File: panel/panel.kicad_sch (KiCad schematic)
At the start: 22 parts

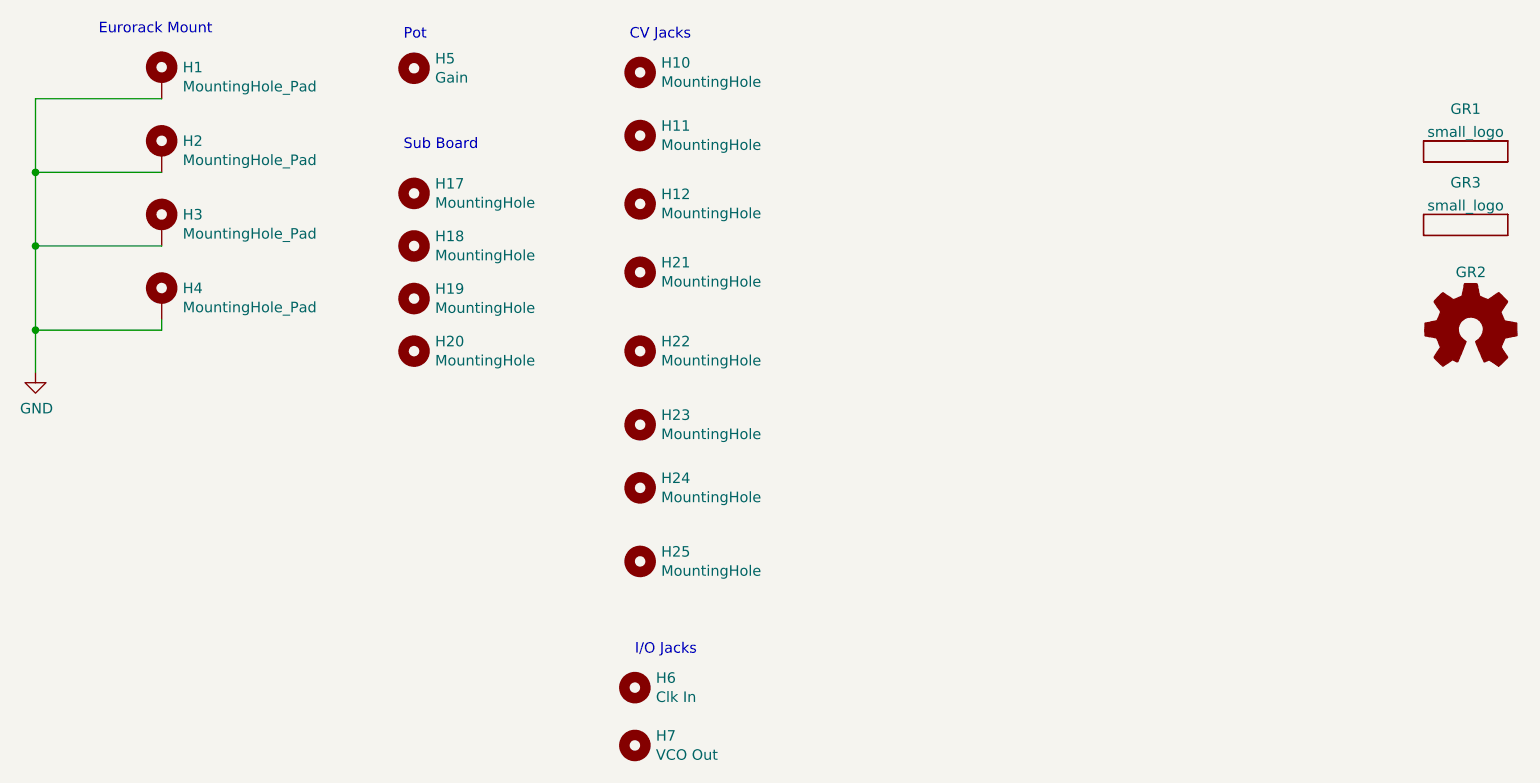
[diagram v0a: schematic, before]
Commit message: Adds harmonic outputs
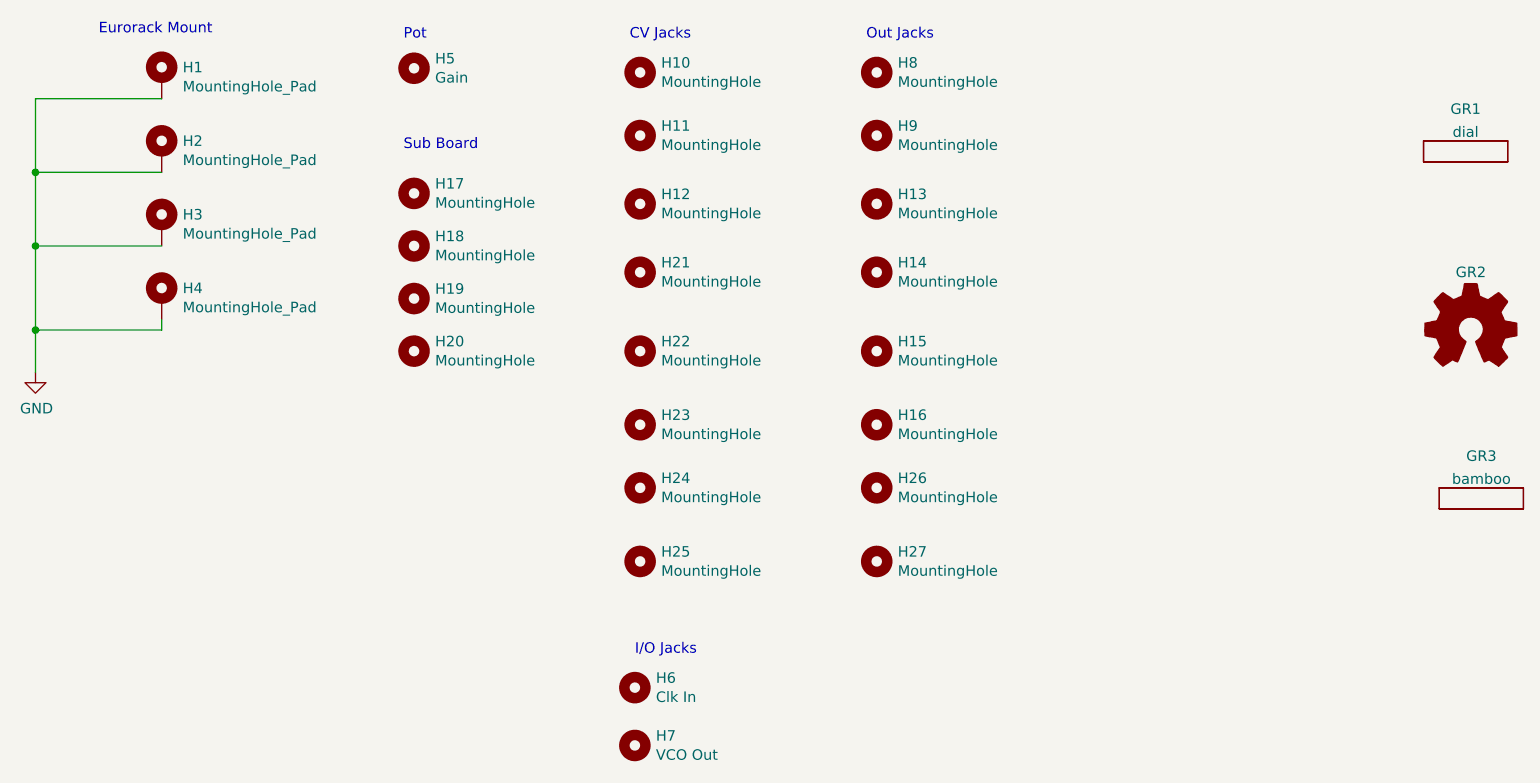
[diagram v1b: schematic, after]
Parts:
- added H13, H14, H15, H16, H26, H27, H8, H9: MountingHole, panel:MolexJack, symbol Mechanical:MountingHole
- GR1: value small_logo -> dial; footprint panel:small_face -> panel:dial_sm
- GR3: value small_logo -> bamboo; footprint Symbol:KiCad-Logo_5mm_SilkScreen -> panel:bambooh
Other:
- note added: "Out Jacks"
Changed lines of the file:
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@@
+    (effects (font (size 1.27 1.27)) (justify left bottom))
+  )
+  (text "Out Jacks" (at 158.75 48.26 0)
     (effects (font (size 1.27 1.27)) (justify left bottom))
   )
@@
     )
   )
+  (symbol (lib_id "Mechanical:MountingHole") (at 160.02 102.235 0) (unit 1)
+    (in_bom yes) (on_board yes)
+    (property "Reference" "H26" (id 0) (at 162.56 101.0666 0)
+      (effects (font (size 1.27 1.27)) (justify left))
+    )
+    (property "Value" "MountingHole" (id 1) (at 162.56 103.378 0)
+      (effects (font (size 1.27 1.27)) (justify left))
+    )
+    (property "Footprint" "panel:MolexJack" (id 2) (at 160.02 102.235 0)
+      (effects (font (size 1.27 1.27)) hide)
+    )
+    (property "Datasheet" "~" (id 3) (at 160.02 102.235 0)
+      (effects (font (size 1.27 1.27)) hide)
+    )
+  )
   (symbol (lib_id "Mechanical:MountingHole_Pad") (at 73.66 52.705 0) (unit 1)
     (in_bom yes) (on_board yes)
@@
     )
   )
+  (symbol (lib_id "Mechanical:MountingHole") (at 160.02 52.07 0) (unit 1)
+    (in_bom yes) (on_board yes)
+    (property "Reference" "H8" (id 0) (at 162.56 50.9016 0)
+      (effects (font (size 1.27 1.27)) (justify left))
+    )
+    (property "Value" "MountingHole" (id 1) (at 162.56 53.213 0)
+      (effects (font (size 1.27 1.27)) (justify left))
+    )
+    (property "Footprint" "panel:MolexJack" (id 2) (at 160.02 52.07 0)
+      (effects (font (size 1.27 1.27)) hide)
+    )
+    (property "Datasheet" "~" (id 3) (at 160.02 52.07 0)
+      (effects (font (size 1.27 1.27)) hide)
+    )
+  )
   (symbol (lib_id "Mechanical:MountingHole") (at 104.14 79.375 0) (unit 1)
     (in_bom yes) (on_board yes)
@@
     )
   )
+  (symbol (lib_id "Mechanical:MountingHole") (at 160.02 67.945 0) (unit 1)
+    (in_bom yes) (on_board yes)
+    (property "Reference" "H13" (id 0) (at 162.56 66.7766 0)
+      (effects (font (size 1.27 1.27)) (justify left))
+    )
+    (property "Value" "MountingHole" (id 1) (at 162.56 69.088 0)
+      (effects (font (size 1.27 1.27)) (justify left))
+    )
+    (property "Footprint" "panel:MolexJack" (id 2) (at 160.02 67.945 0)
+      (effects (font (size 1.27 1.27)) hide)
+    )
+    (property "Datasheet" "~" (id 3) (at 160.02 67.945 0)
+      (effects (font (size 1.27 1.27)) hide)
+    )
+  )
   (symbol (lib_id "Mechanical:MountingHole") (at 131.445 102.235 0) (unit 1)
     (in_bom yes) (on_board yes)
@@
     )
   )
+  (symbol (lib_id "Mechanical:MountingHole") (at 160.02 111.125 0) (unit 1)
+    (in_bom yes) (on_board yes)
+    (property "Reference" "H27" (id 0) (at 162.56 109.9566 0)
+      (effects (font (size 1.27 1.27)) (justify left))
+    )
+    (property "Value" "MountingHole" (id 1) (at 162.56 112.268 0)
+      (effects (font (size 1.27 1.27)) (justify left))
+    )
+    (property "Footprint" "panel:MolexJack" (id 2) (at 160.02 111.125 0)
+      (effects (font (size 1.27 1.27)) hide)
+    )
+    (property "Datasheet" "~" (id 3) (at 160.02 111.125 0)
+      (effects (font (size 1.27 1.27)) hide)
+    )
+  )
   (symbol (lib_id "Mechanical:MountingHole_Pad") (at 73.66 61.595 0) (unit 1)
     (in_bom yes) (on_board yes)
@@
     (pin "1")
   )
+  (symbol (lib_id "Mechanical:MountingHole") (at 160.02 94.615 0) (unit 1)
+    (in_bom yes) (on_board yes)
+    (property "Reference" "H16" (id 0) (at 162.56 93.4466 0)
+      (effects (font (size 1.27 1.27)) (justify left))
+    )
+    (property "Value" "MountingHole" (id 1) (at 162.56 95.758 0)
+      (effects (font (size 1.27 1.27)) (justify left))
+    )
+    (property "Footprint" "panel:MolexJack" (id 2) (at 160.02 94.615 0)
+      (effects (font (size 1.27 1.27)) hide)
+    )
+    (property "Datasheet" "~" (id 3) (at 160.02 94.615 0)
+      (effects (font (size 1.27 1.27)) hide)
+    )
+  )
   (symbol (lib_id "Mechanical:MountingHole") (at 131.445 94.615 0) (unit 1)
     (in_bom yes) (on_board yes)
@@
     )
     (property "Datasheet" "~" (id 3) (at 131.445 94.615 0)
+      (effects (font (size 1.27 1.27)) hide)
+    )
+  )
+  (symbol (lib_id "Mechanical:MountingHole") (at 160.02 85.725 0) (unit 1)
+    (in_bom yes) (on_board yes)
+    (property "Reference" "H15" (id 0) (at 162.56 84.5566 0)
+      (effects (font (size 1.27 1.27)) (justify left))
+    )
+    (property "Value" "MountingHole" (id 1) (at 162.56 86.868 0)
+      (effects (font (size 1.27 1.27)) (justify left))
+    )
+    (property "Footprint" "panel:MolexJack" (id 2) (at 160.02 85.725 0)
+      (effects (font (size 1.27 1.27)) hide)
+    )
+    (property "Datasheet" "~" (id 3) (at 160.02 85.725 0)
       (effects (font (size 1.27 1.27)) hide)
     )
@@
     (in_bom yes) (on_board yes) (fields_autoplaced)
     (property "Reference" "GR1" (id 0) (at 231.14 56.4855 0))
-    (property "Value" "small_logo" (id 1) (at 231.14 59.2606 0))
-    (property "Footprint" "panel:small_face" (id 2) (at 231.14 61.595 0)
+    (property "Value" "dial" (id 1) (at 231.14 59.2606 0))
+    (property "Footprint" "panel:dial_sm" (id 2) (at 231.14 61.595 0)
       (effects (font (size 1.27 1.27)) hide)
     )
@@
     )
   )
+  (symbol (lib_id "greenface-symbols:small_logo") (at 233.045 103.505 0) (unit 1)
+    (in_bom yes) (on_board yes) (fields_autoplaced)
+    (property "Reference" "GR3" (id 0) (at 233.045 98.3955 0))
+    (property "Value" "bamboo" (id 1) (at 233.045 101.1706 0))
+    (property "Footprint" "panel:bambooh" (id 2) (at 233.045 103.505 0)
+      (effects (font (size 1.27 1.27)) hide)
+    )
+    (property "Datasheet" "" (id 3) (at 233.045 103.505 0)
+      (effects (font (size 1.27 1.27)) hide)
+    )
+  )
+  (symbol (lib_id "Mechanical:MountingHole") (at 160.02 76.2 0) (unit 1)
+    (in_bom yes) (on_board yes)
+    (property "Reference" "H14" (id 0) (at 162.56 75.0316 0)
+      (effects (font (size 1.27 1.27)) (justify left))
+    )
+    (property "Value" "MountingHole" (id 1) (at 162.56 77.343 0)
+      (effects (font (size 1.27 1.27)) (justify left))
+    )
+    (property "Footprint" "panel:MolexJack" (id 2) (at 160.02 76.2 0)
+      (effects (font (size 1.27 1.27)) hide)
+    )
+    (property "Datasheet" "~" (id 3) (at 160.02 76.2 0)
+      (effects (font (size 1.27 1.27)) hide)
+    )
+  )
   (symbol (lib_id "Mechanical:MountingHole") (at 130.81 133.35 0) (unit 1)
     (in_bom yes) (on_board yes)
@@
     )
   )
-  (symbol (lib_id "greenface-symbols:small_logo") (at 231.14 70.485 0) (unit 1)
-    (in_bom yes) (on_board yes) (fields_autoplaced)
-    (property "Reference" "GR3" (id 0) (at 231.14 65.3755 0))
-    (property "Value" "small_logo" (id 1) (at 231.14 68.1506 0))
-    (property "Footprint" "Symbol:KiCad-Logo_5mm_SilkScreen" (id 2) (at 231.14 70.485 0)
-      (effects (font (size 1.27 1.27)) hide)
-    )
-    (property "Datasheet" "" (id 3) (at 231.14 70.485 0)
+  (symbol (lib_id "Mechanical:MountingHole") (at 160.02 59.69 0) (unit 1)
+    (in_bom yes) (on_board yes)
+    (property "Reference" "H9" (id 0) (at 162.56 58.5216 0)
+      (effects (font (size 1.27 1.27)) (justify left))
+    )
+    (property "Value" "MountingHole" (id 1) (at 162.56 60.833 0)
+      (effects (font (size 1.27 1.27)) (justify left))
+    )
+    (property "Footprint" "panel:MolexJack" (id 2) (at 160.02 59.69 0)
+      (effects (font (size 1.27 1.27)) hide)
+    )
+    (property "Datasheet" "~" (id 3) (at 160.02 59.69 0)
       (effects (font (size 1.27 1.27)) hide)
     )
@@
     )
     (path "/b7e9d1ed-d010-49fa-95b8-39eee642e6e7"
-      (reference "GR1") (unit 1) (value "small_logo") (footprint "panel:small_face")
+      (reference "GR1") (unit 1) (value "dial") (footprint "panel:dial_sm")
     )
     (path "/307d06a5-a22d-4946-8b80-4f092fd73e46"
       (reference "GR2") (unit 1) (value "Logo_Open_Hardware_Small") (footprint "Symbol:OSHW-Logo_5.7x6mm_SilkScreen")
     )
-    (path "/e52387aa-9a3c-4f08-b265-477019aca115"
-      (reference "GR3") (unit 1) (value "small_logo") (footprint "Symbol:KiCad-Logo_5mm_SilkScreen")
+    (path "/bd6f6aaa-569a-4c75-a8ff-b09aedaec1f5"
+      (reference "GR3") (unit 1) (value "bamboo") (footprint "panel:bambooh")
     )
     (path "/495b9f3e-72d4-4443-8d1b-2b95612acb36"
@@
       (reference "H7") (unit 1) (value "VCO Out") (footprint "panel:MolexJack")
     )
+    (path "/6437bf88-0b99-43e2-818e-fdd13eae6b91"
+      (reference "H8") (unit 1) (value "MountingHole") (footprint "panel:MolexJack")
+    )
+    (path "/e109b36d-0314-4232-b3e9-6076fc13043d"
+      (reference "H9") (unit 1) (value "MountingHole") (footprint "panel:MolexJack")
+    )
     (path "/55439d6c-cdf1-4cc6-9c90-3dbefeda32d9"
       (reference "H10") (unit 1) (value "MountingHole") (footprint "panel:MolexJack")
@@
       (reference "H12") (unit 1) (value "MountingHole") (footprint "panel:MolexJack")
     )
+    (path "/6a3b37dc-b091-4334-ab9f-7817f4ad7174"
+      (reference "H13") (unit 1) (value "MountingHole") (footprint "panel:MolexJack")
+    )
+    (path "/c477bd89-c5cf-45a5-bad0-aa9992e513c3"
+      (reference "H14") (unit 1) (value "MountingHole") (footprint "panel:MolexJack")
+    )
+    (path "/b4e75807-63a7-4715-9870-250e5e8e8144"
+      (reference "H15") (unit 1) (value "MountingHole") (footprint "panel:MolexJack")
+    )
+    (path "/a5d63e6a-ea2a-4b49-8716-3c4ef63b9fff"
+      (reference "H16") (unit 1) (value "MountingHole") (footprint "panel:MolexJack")
+    )
     (path "/40f359aa-e8bc-4d4c-ab4e-c4039d94c199"
       (reference "H17") (unit 1) (value "MountingHole") (footprint "MountingHole:MountingHole_2.5mm")
@@
       (reference "H25") (unit 1) (value "MountingHole") (footprint "panel:MolexJack")
     )
-  )
+    (path "/4178e207-1476-4b91-9526-2b553791f86e"
+      (reference "H26") (unit 1) (value "MountingHole") (footprint "panel:MolexJack")
+    )
+    (path "/91bfe3fd-d346-4974-9300-6641d430ee08"
+      (reference "H27") (unit 1) (value "MountingHole") (footprint "panel:MolexJack")
+    )
+  )

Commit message: Adds digikey bom merge. Uses local graphics for panel.
Adds bambooh graphics
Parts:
- GR3: footprint panel:bambooh -> pipes:bambooh
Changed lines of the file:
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@@
     (property "Reference" "GR3" (id 0) (at 233.045 98.3955 0))
     (property "Value" "bamboo" (id 1) (at 233.045 101.1706 0))
-    (property "Footprint" "panel:bambooh" (id 2) (at 233.045 103.505 0)
+    (property "Footprint" "pipes:bambooh" (id 2) (at 233.045 103.505 0)
       (effects (font (size 1.27 1.27)) hide)
     )
@@
     )
     (path "/bd6f6aaa-569a-4c75-a8ff-b09aedaec1f5"
-      (reference "GR3") (unit 1) (value "bamboo") (footprint "panel:bambooh")
+      (reference "GR3") (unit 1) (value "bamboo") (footprint "pipes:bambooh")
     )
     (path "/495b9f3e-72d4-4443-8d1b-2b95612acb36"

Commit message: Version 1.1 of boards
Changes to use NSL-32SR3 Vactrols
Fixes 3904 package
Adds 10-step waveform
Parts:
- GR1: footprint panel:dial_sm -> panel:dial2
- H5: footprint panel:RotaryEncoder_6.4mm -> panel:Potentiometer_Bourns_PTV09A-1_Single_Vertical
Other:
- title: Bonkulator Panel -> Pipes Panel
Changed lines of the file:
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@@
   (paper "A4")
   (title_block
-    (title "Bonkulator Panel")
-    (rev "2.1")
+    (title "Pipes Panel")
+    (rev "1.1")
   )
   (junction (at 58.42 64.135) (diameter 0) (color 0 0 0 0)
@@
     (property "Reference" "GR1" (id 0) (at 231.14 56.4855 0))
     (property "Value" "dial" (id 1) (at 231.14 59.2606 0))
-    (property "Footprint" "panel:dial_sm" (id 2) (at 231.14 61.595 0)
+    (property "Footprint" "panel:dial2" (id 2) (at 231.14 61.595 0)
       (effects (font (size 1.27 1.27)) hide)
     )
@@
       (effects (font (size 1.27 1.27)) (justify left))
     )
-    (property "Footprint" "panel:RotaryEncoder_6.4mm" (id 2) (at 104.14 51.562 0)
+    (property "Footprint" "panel:Potentiometer_Bourns_PTV09A-1_Single_Vertical" (id 2) (at 104.14 51.562 0)
       (effects (font (size 1.27 1.27)) hide)
     )
@@
     )
     (path "/b7e9d1ed-d010-49fa-95b8-39eee642e6e7"
-      (reference "GR1") (unit 1) (value "dial") (footprint "panel:dial_sm")
+      (reference "GR1") (unit 1) (value "dial") (footprint "panel:dial2")
     )
     (path "/307d06a5-a22d-4946-8b80-4f092fd73e46"
@@
     )
     (path "/bcb71876-c270-45b1-942b-f8b7b2e74527"
-      (reference "H5") (unit 1) (value "Gain") (footprint "panel:RotaryEncoder_6.4mm")
+      (reference "H5") (unit 1) (value "Gain") (footprint "panel:Potentiometer_Bourns_PTV09A-1_Single_Vertical")
     )
     (path "/b8f3be1f-4f7f-41d5-b496-5f7052d6e8e5"
